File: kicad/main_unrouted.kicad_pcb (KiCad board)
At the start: 2 copper layers, 200 x 100 mm, 48 parts, among them J1 Barrel_Jack, J2 UART, P1 Mini-DIN_6pins_ver3, SW1 Reset, SW2 SW_Push_DPDT, U1 KM1810VM88, U10 L7805, U11 15 MHz, U12 8255, U13 uSD adapter, U14 8259, U15 AS6C4008-55PCN, U16 16550, U17 T6963C, U18 1.8432 MHz, U19 ATF16V8, U2 W27C512, U3 AS6C4008-55PCN, U4 74HC573, U5 74HC573, U6 ATF16V8, U7 DS1813-5+, U8 74HC14, U9 8253

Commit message: Even better PCB
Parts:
- moved U9 29.0 mm to (94.0, 86.4), turned to 0 degrees
- moved C8 25.9 mm to (95.2, 74.9), turned to 0 degrees
- moved U14 22.7 mm to (116.8, 81.3), turned to 0 degrees
- moved U8 21.7 mm to (94.0, 78.7), turned to 90 degrees
- moved C12 20.1 mm to (124.5, 90.2), turned to -90 degrees
- moved RN1 14.9 mm to (25.4, 68.6), turned to 90 degrees
- moved C10 14.8 mm to (101.6, 94.0), turned to -90 degrees
- moved C11 5.68 mm to (30.5, 100.3)
- moved U2 5.68 mm to (43.2, 109.2)
- moved J2 2.84 mm to (153.7, 114.3)
- moved U11 2.54 mm to (149.9, 103.0)

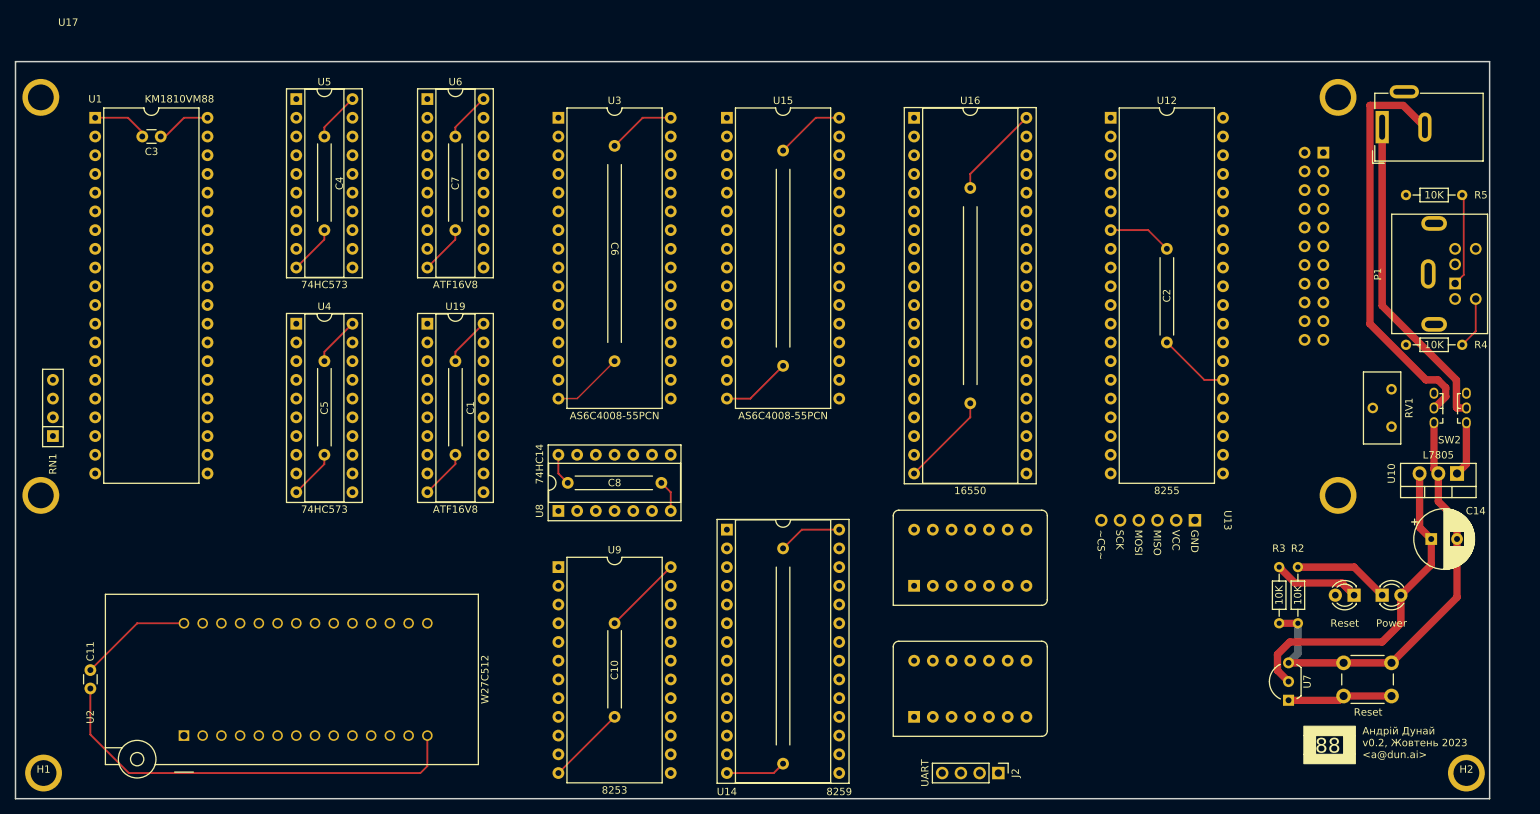
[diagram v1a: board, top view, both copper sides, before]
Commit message: New PCB (add MCB line)
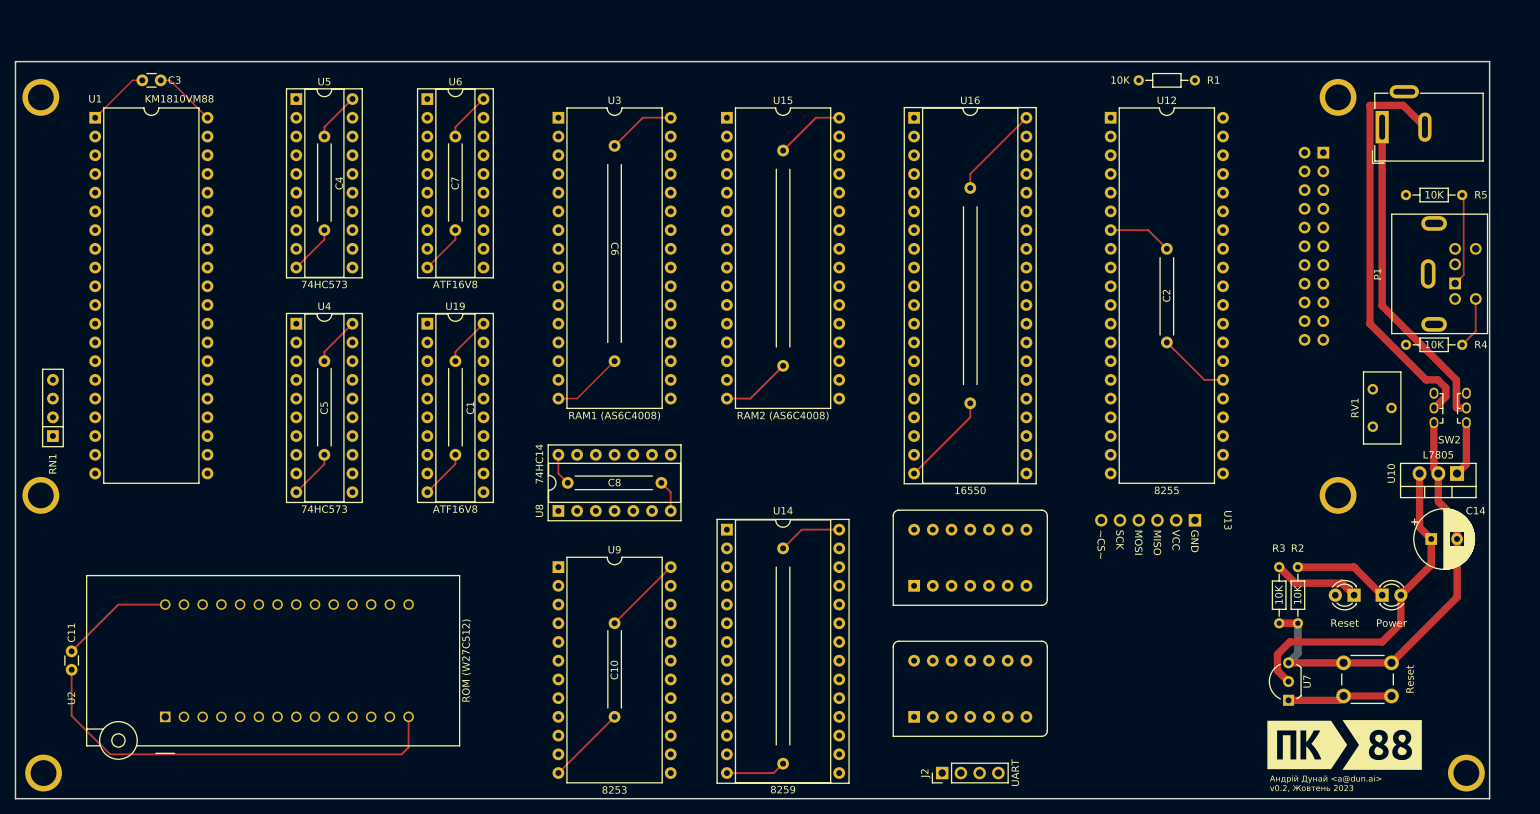
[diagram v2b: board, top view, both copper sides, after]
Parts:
- added R1: 10K, Resistor_THT:R_Axial_DIN0204_L3.6mm_D1.6mm_P7.62mm_Horizontal, F.Cu at (180.3, 20.3)
- added kibuzzard-65254FD7: G***, kibuzzard-65254FD7, F.Cu at (195.6, 110.5)
- added kibuzzard-65254FDB: G***, kibuzzard-65254FDB, F.Cu at (205.7, 110.5)
- U15: value AS6C4008-55PCN -> RAM2 (AS6C4008)
- U2: value W27C512 -> ROM (W27C512)
- U3: value AS6C4008-55PCN -> RAM1 (AS6C4008)
- moved C3 7.62 mm to (40.0, 20.3)
- moved J2 7.62 mm to (146.1, 114.3), turned to 90 degrees
- moved RV1 5.68 mm to (204.5, 62.2), turned to 90 degrees
- moved C11 3.59 mm to (27.9, 97.8)
- moved U2 3.59 mm to (40.6, 106.7)
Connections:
- U12 pad 4: unconnected-(U12-PA0-Pad4) -> MCB
- U6 pad 7: unconnected-(U6-I-Pad7) -> MCB
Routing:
- net GND: track 216.5 -> 217.6 mm
- net +5V: track 159.7 -> 160.7 mm
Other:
- board text added: "Андрій Дунай <a@dun.ai> v0.2, Жовтень 2023"
- board text removed: "88"
- board text removed: "Андрій Дунай v0.2, Жовтень 2023 <a@dun.ai>"

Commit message: WIP: PCB v3.0
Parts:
- added BZ1: Buzzer, Buzzer_Beeper:Buzzer_TDK_PS1240P02BT_D12.2mm_H6.5mm, F.Cu at (94.1, 109.2)
- added C15: 0.1 uF, footprints:C_Disc_Long, F.Cu at (234.9, 86.4)
- added H3: MountingHole, footprints:Hole_3.5x5, F.Cu at (254.0, 121.9)
- added KB1: ATF22V10, Package_DIP:DIP-24_W7.62mm_Socket, F.Cu at (231.1, 78.7)
- added R6: 10K, Resistor_THT:R_Axial_DIN0204_L3.6mm_D1.6mm_P7.62mm_Horizontal, F.Cu at (92.7, 99.1)
- moved H2 98.6 mm to (254.0, 22.9)
- moved J2 96.7 mm to (168.9, 20.3)
- moved R5 82.1 mm to (255.6, 103.4), turned to 180 degrees
- moved C14 67.2 mm to (241.3, 21.9), turned to -90 degrees
- moved R1 65.6 mm to (228.6, 64.8), turned to -90 degrees
- moved D1 57.4 mm to (252.7, 57.1)
- moved D2 57.4 mm to (248.9, 57.1)
- moved SW1 57.3 mm to (254.0, 71.1)
- moved P1 54.8 mm to (248.9, 91.4), turned to 90 degrees
- moved U3 54.5 mm to (236.2, 71.1)
- moved R4 53.8 mm to (255.6, 83.1), turned to 180 degrees
- moved R3 49.3 mm to (232.4, 58.4), turned to 0 degrees
- moved R2 48.8 mm to (232.4, 55.9), turned to 0 degrees
- moved SW2 46.4 mm to (257.2, 51.1), turned to 180 degrees
- moved RV1 40.8 mm to (208.3, 21.6)
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- renumbered U4 to ADDR1, U5 to ADDR2, U1 to CPU1, U6 to DEC1, U19 to DEC2, U17 to LCD1, U14 to PIC1, U9 to PIT1, U12 to PPI1, U3 to RAM1, U15 to RAM2, U2 to ROM1, U13 to SD1, U10 to U1, U8 to U2, U7 to U3, U16 to UART1, U11 to X1, U18 to X2
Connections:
- DEC1 pad 12: unconnected-(U6-I/O-Pad12) -> SPKROUT
- DEC1 pad 8: unconnected-(U6-I-Pad8) -> T2OUT
- DEC1 pad 9: unconnected-(U6-I-Pad9) -> SPKREN
- DEC2 pad 14: unconnected-(U19-I/O-Pad14) -> PS2~{EN}
- PIT1 pad 16: unconnected-(U9-G2-Pad16) -> T2GATE
- PIT1 pad 17: unconnected-(U9-OUT2-Pad17) -> T2OUT
- PIT1 pad 18: unconnected-(U9-CLK2-Pad18) -> TIMERCLK
- PPI1 pad 11: unconnected-(U12-PC6-Pad11) -> Net-(PPI1-PC6)
- PPI1 pad 12: unconnected-(U12-PC5-Pad12) -> Net-(PPI1-PC5)
- PPI1 pad 13: unconnected-(U12-PC4-Pad13) -> Net-(PPI1-PC4)
- PPI1 pad 14: INT1 -> Net-(PPI1-PC0)
- PPI1 pad 16: PS2CLK -> unconnected-(PPI1-PC2-Pad16)
- PPI1 pad 18: PS2DATA -> T2GATE
- PPI1 pad 19: unconnected-(U12-PB1-Pad19) -> SPKREN
- PPI1 pad 22: unconnected-(U12-PB4-Pad22) -> MCB
- PPI1 pad 4: MCB -> unconnected-(PPI1-PA0-Pad4)
- SD1 pad 3: Net-(U13-MISO) -> Net-(PPI1-PC0)
- SD1 pad 4: Net-(U13-MOSI) -> Net-(PPI1-PC4)
- SD1 pad 5: Net-(U13-SCK) -> Net-(PPI1-PC5)
- SD1 pad 6: Net-(U13-~{CS}) -> Net-(PPI1-PC6)
- UART1 pad 32: Net-(U13-~{CS}) -> unconnected-(UART1-~{RTS}-Pad32)
- UART1 pad 33: Net-(U13-SCK) -> unconnected-(UART1-~{DTR}-Pad33)
- UART1 pad 34: Net-(U13-MOSI) -> unconnected-(UART1-~{OUT1}-Pad34)
- UART1 pad 36: Net-(U13-MISO) -> unconnected-(UART1-~{CTS}-Pad36)
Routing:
- net Net-(J1-Pad2): track 55.6 -> 0.00 mm
- net Net-(J1-Pad1): track 43.6 -> 0.00 mm
- net GND: track 217.6 -> 180.2 mm
- net +5V: track 160.7 -> 125.2 mm
- net ~{RES}: track 14.2 -> 0.00 mm
- net Net-(D1-K): track 13.0 -> 0.00 mm
- net PS2DATA: track 12.6 -> 0.00 mm
- net Net-(D2-K): track 11.7 -> 0.00 mm
- net Net-(U1-IN): track 7.42 -> 0.00 mm
- net PS2CLK: track 6.98 -> 0.00 mm
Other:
- board size 200 x 100 mm -> 238.8 x 109.2 mm
- board text added: "Андрій Дунай <a@dun.ai> v0.3, Листопад 2023"
- board text removed: "Андрій Дунай <a@dun.ai> v0.2, Жовтень 2023"

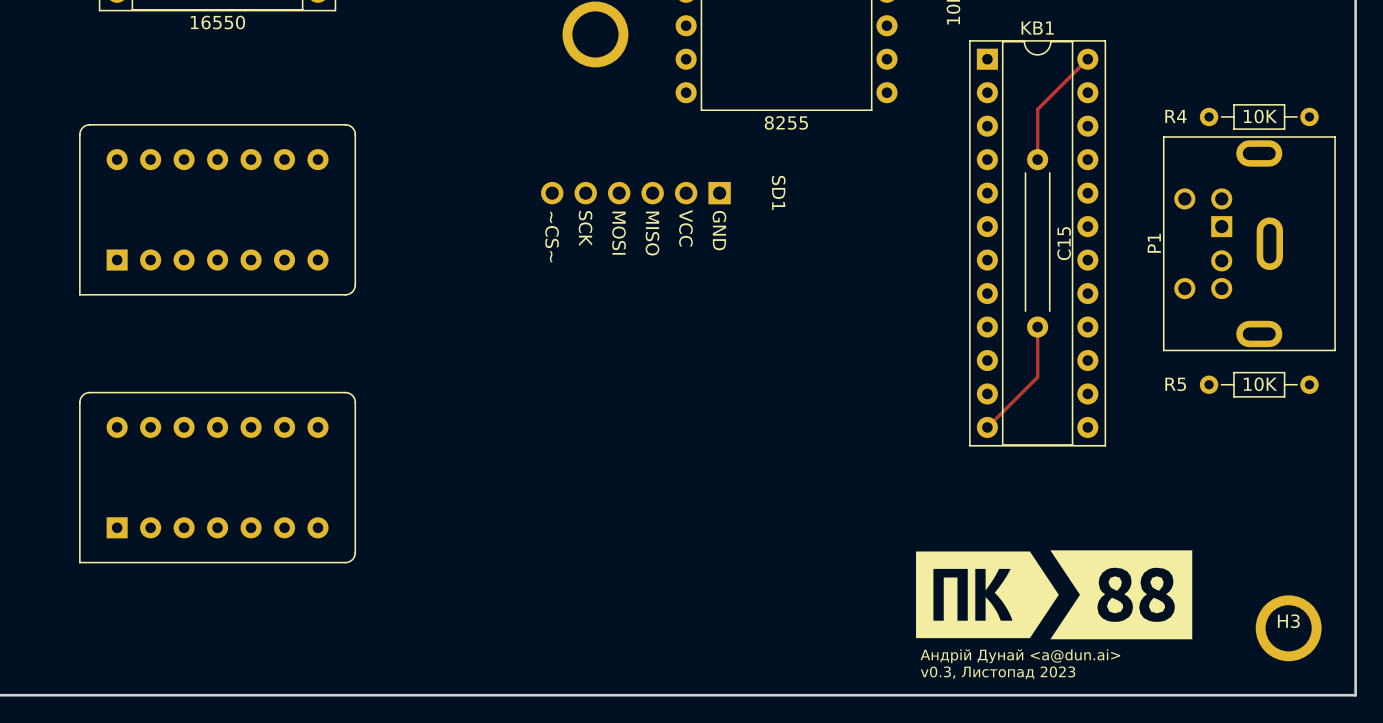
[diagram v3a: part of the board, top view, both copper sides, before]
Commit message: Add SPI controller to PCB v0.3
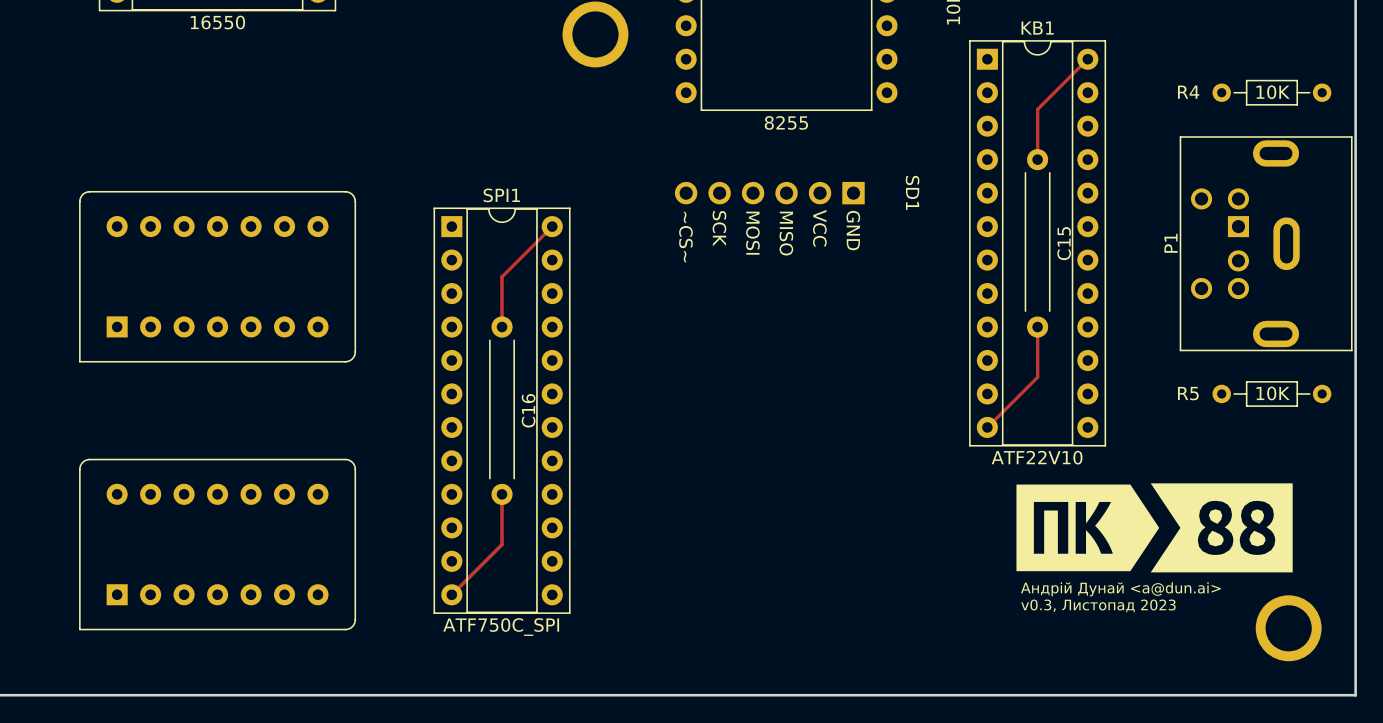
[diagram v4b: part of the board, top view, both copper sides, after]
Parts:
- added C16: 0.1 uF, footprints:C_Disc_Long, F.Cu at (194.3, 99.1)
- added SPI1: ATF750C_SPI, Package_DIP:DIP-24_W7.62mm_Socket, F.Cu at (190.5, 91.4)
- moved SD1 10.2 mm to (226.7, 86.4)
- moved kibuzzard-65254FD7 9.16 mm to (238.8, 114.3)
- moved kibuzzard-65254FDB 9.16 mm to (248.9, 114.3)
- moved X2 5.08 mm to (172.7, 95.4)
- moved X1 5.08 mm to (172.7, 115.7)
- moved R4 2.08 mm to (256.5, 81.3)
- moved P1 1.27 mm to (250.2, 91.4)
- moved R5 1.19 mm to (256.5, 104.1)
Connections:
- DEC2 pad 13: unconnected-(DEC2-I/O-Pad13) -> SPI~{EN}
- LCD1 pad 1: (no net) -> unconnected-(LCD1-NC-Pad1)
- LCD1 pad 10: (no net) -> unconnected-(LCD1-NC-Pad10)
- LCD1 pad 9: (no net) -> unconnected-(LCD1-NC-Pad9)
- PPI1 pad 11: Net-(PPI1-PC6) -> unconnected-(PPI1-PC6-Pad11)
- PPI1 pad 12: Net-(PPI1-PC5) -> unconnected-(PPI1-PC5-Pad12)
- PPI1 pad 13: Net-(PPI1-PC4) -> unconnected-(PPI1-PC4-Pad13)
- PPI1 pad 14: Net-(PPI1-PC0) -> unconnected-(PPI1-PC0-Pad14)
- PPI1 pad 23: unconnected-(PPI1-PB5-Pad23) -> SD~{CS}
- SD1 pad 3: Net-(PPI1-PC0) -> Net-(SD1-MISO)
- SD1 pad 4: Net-(PPI1-PC4) -> Net-(SD1-MOSI)
- SD1 pad 5: Net-(PPI1-PC5) -> Net-(SD1-SCK)
- SD1 pad 6: Net-(PPI1-PC6) -> SD~{CS}
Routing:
- net GND: track 180.2 -> 189.4 mm
- net +5V: track 125.2 -> 134.4 mm

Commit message: WIP - PCB v0.4
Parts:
- added H4: MountingHole, footprints:Hole_3.5x5, F.Cu at (22.9, 121.9)
- LCD1: footprint footprints:LCD24064 -> footprints:LCD240128_TFT_var2
- moved kibuzzard-65254FD7 205.8 mm to (33.0, 119.4)
- moved kibuzzard-65254FDB 205.8 mm to (43.2, 119.4)
- moved RV1 133.9 mm to (116.8, 119.4), turned to 0 degrees
- moved H1 99.1 mm to (22.9, 22.9)
- moved C11 80.1 mm to (36.8, 25.4), turned to 180 degrees
- moved C10 79.1 mm to (35.6, 91.4)
- moved PIT1 79.1 mm to (27.9, 83.8)
- moved ROM1 78.2 mm to (27.9, 38.1), turned to 0 degrees
- moved C12 73.7 mm to (68.6, 92.7)
- moved PIC1 73.7 mm to (61.0, 83.8)
- moved SW1 66.2 mm to (214.9, 124.5)
- moved R2 66.1 mm to (229.9, 121.9), turned to 180 degrees
- moved C1 62.3 mm to (149.9, 76.2)
- moved DEC2 62.3 mm to (146.1, 71.1)
- moved R3 61.0 mm to (229.9, 119.4), turned to 180 degrees
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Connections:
- KB1 pad 14: AD_{7} -> unconnected-(KB1-O-Pad14)
- KB1 pad 15: AD_{6} -> AD_{0}
- KB1 pad 16: AD_{5} -> AD_{1}
- KB1 pad 17: AD_{4} -> AD_{2}
- KB1 pad 19: AD_{2} -> AD_{4}
- KB1 pad 20: AD_{1} -> AD_{5}
- KB1 pad 21: AD_{0} -> AD_{6}
- KB1 pad 22: unconnected-(KB1-O-Pad22) -> AD_{7}
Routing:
- net GND: track 189.4 -> 186.4 mm
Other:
- board size 238.8 x 109.2 mm -> 228.6 x 109.2 mm
